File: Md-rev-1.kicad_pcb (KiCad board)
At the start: 2 copper layers, 50 x 21.5 mm, 29 parts, among them J1 USB_C_Receptacle_USB2.0, J2 54-00177, U1 MCP73831-2-OT, U2 MAX9814

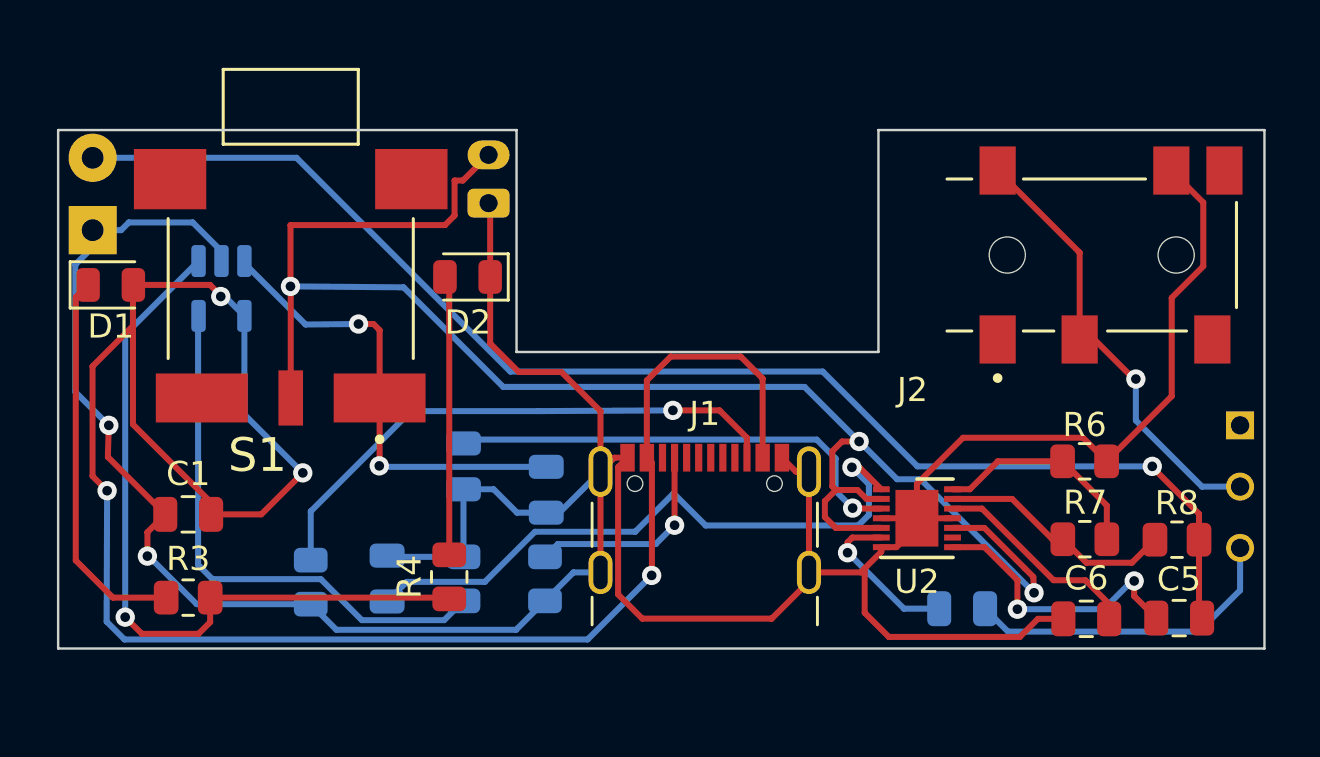
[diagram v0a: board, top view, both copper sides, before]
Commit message: swapping out the usb connector
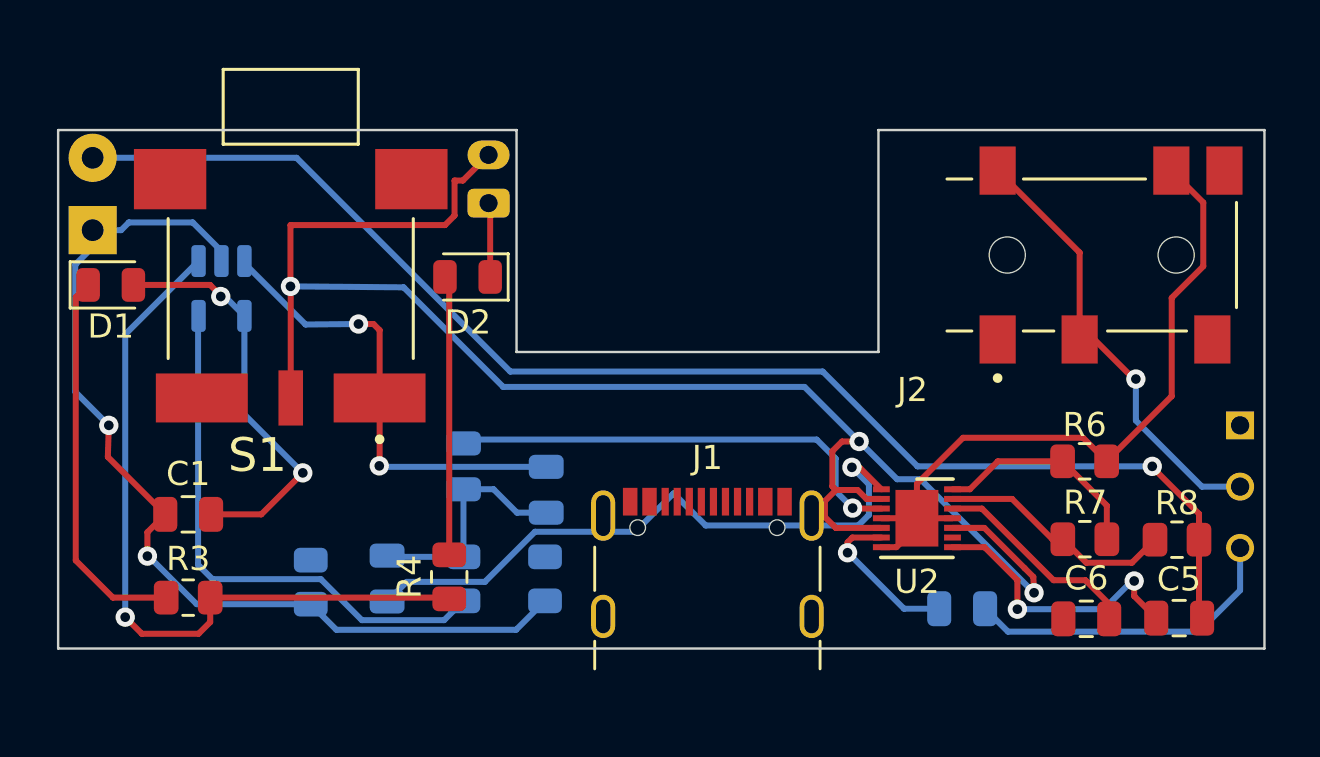
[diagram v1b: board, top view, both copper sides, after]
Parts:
- moved J1 1.83 mm to (156.9, 123.2)
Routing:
- net /5V: track 82.8 -> 17.7 mm, vias 4 -> 2
- net GND: track 141.7 -> 84.4 mm
- net Net-(J1-CC2): track 23.2 -> 0.00 mm, vias 1 -> 0
- net Net-(J1-CC1): track 8.71 -> 0.00 mm, vias 1 -> 0

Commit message: adjusted the placement of the usbc
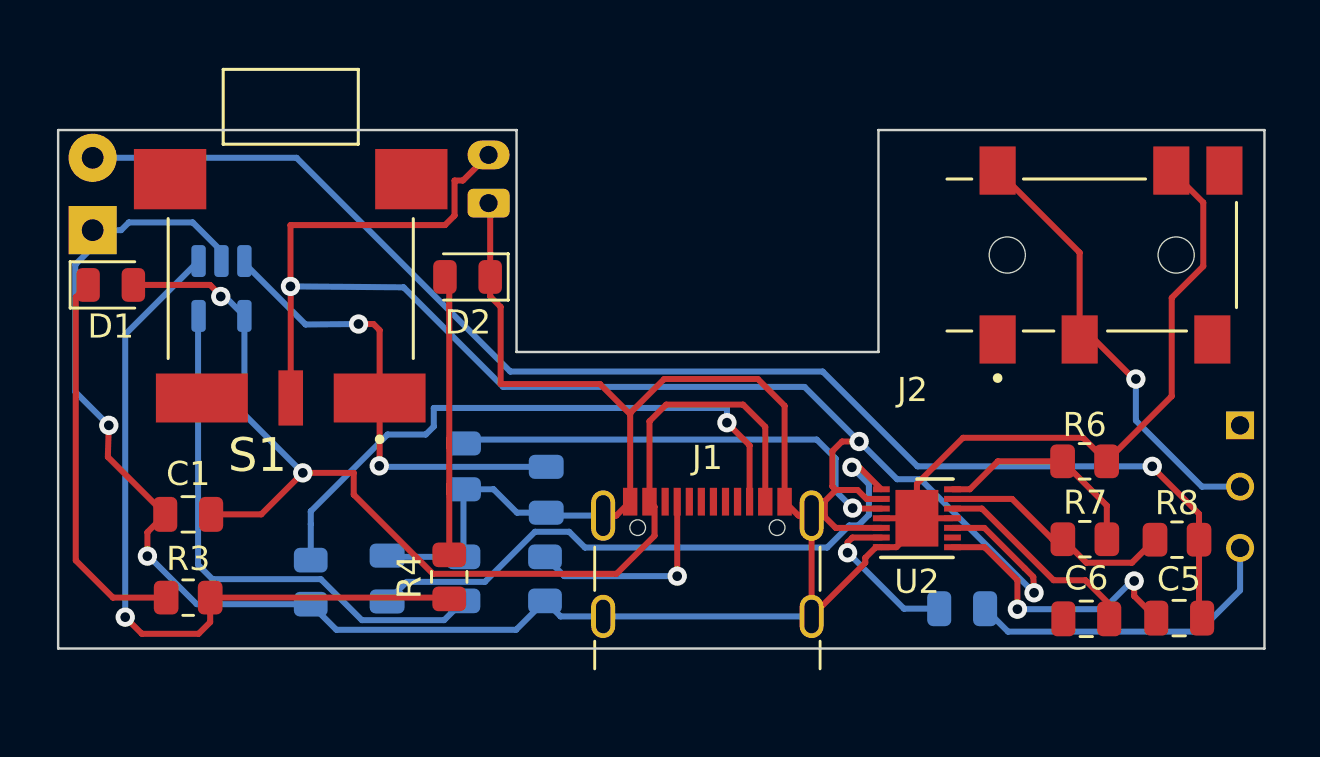
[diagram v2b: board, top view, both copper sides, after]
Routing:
- net GND: track 84.4 -> 134.8 mm
- net /5V: track 17.7 -> 48.6 mm
- net Net-(J1-CC2): track 0.00 -> 25.8 mm, vias 0 -> 1
- net Net-(J1-CC1): track 0.00 -> 8.90 mm, vias 0 -> 1
- net Net-(U2-CT): track 26.5 -> 25.9 mm

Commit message: updated gerberfiles and symbols
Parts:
- removed the ? at (179.0, 121.5)
- removed the ? at (147.8, 107.2)
- removed the ? at (179.0, 116.4)
- removed the ? at (147.8, 105.2)
- removed the ? at (131.4, 105.3)
- removed the ? at (131.4, 108.3)
- removed the ? at (179.0, 118.9)
- added ?: , , F.Cu at (179.0, 118.9)
- added ?: , , F.Cu at (147.9, 107.5)
- added ?: , , F.Cu at (179.0, 116.4)
- added ?: , , F.Cu at (131.3, 105.2)
- added ?: , , F.Cu at (179.0, 121.5)
- added ?: , , F.Cu at (147.9, 105.5)
- added ?: , , F.Cu at (131.3, 107.8)
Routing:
- net GND: track 134.8 -> 134.2 mm
- added copper zone on F.Cu, net GND
